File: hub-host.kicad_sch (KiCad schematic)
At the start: 30 parts, among them J1 USB-C USB2.0, Q2 2N7002, U2 USBLC6-2SC6, U22 TLV75533PDBVR, U24 SN74LVC1G04DBVR, U26 TPS2553DBVR, U3 TUSB320LAIRWBR, U45 TLV62568DBVR

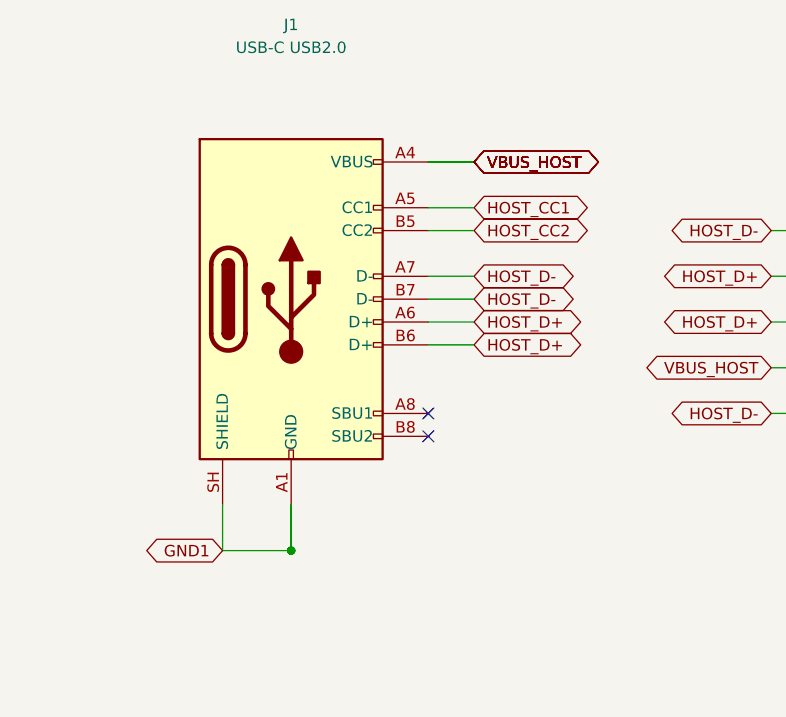
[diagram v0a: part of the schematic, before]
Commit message: feat(revc): assign exact BOM and verified local land patterns
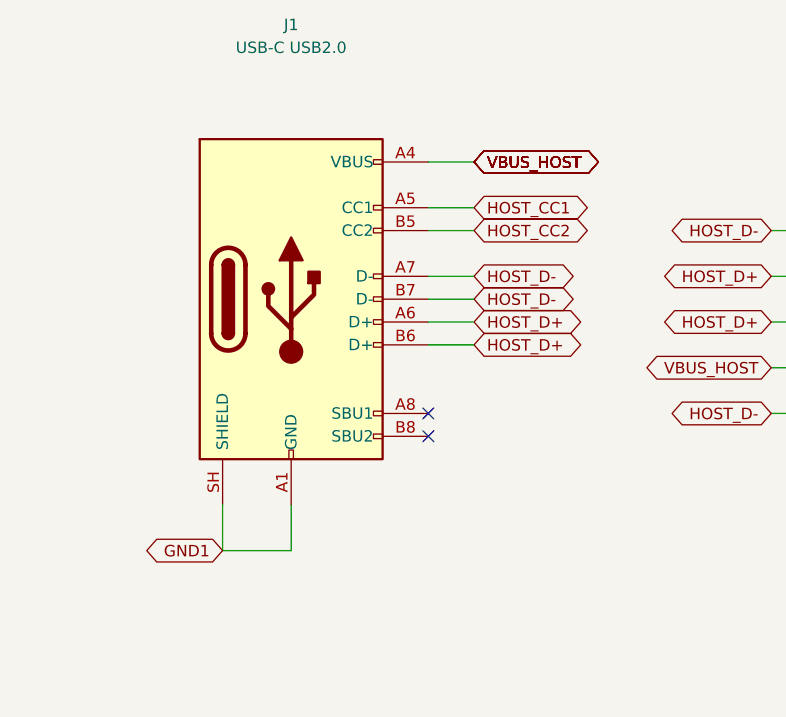
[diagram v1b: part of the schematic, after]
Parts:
- C1, C62, C7, C8: footprint (none) -> hub-lib:C_0402_1005Metric; LCSC (none) -> C77020; MPN (none) -> GRM155R71H104KE14D; Manufacturer (none) -> Murata Manufacturing; Ratings (none) -> 50V X7R 10%
- C113: footprint (none) -> hub-lib:C_0805_2012Metric; LCSC (none) -> C77077; MPN (none) -> GRM21BR61E475KA12L; Manufacturer (none) -> Murata Manufacturing; Ratings (none) -> 25V X5R 10%
- C114: footprint (none) -> hub-lib:C_1210_3225Metric; LCSC (none) -> C21397; MPN (none) -> GRM32ER71E226KE15L; Manufacturer (none) -> Murata Manufacturing; Ratings (none) -> 25V X7R 10%
- C2, C61: footprint (none) -> hub-lib:C_0603_1608Metric; LCSC (none) -> C77046; MPN (none) -> GRM188R61E105KA12D; Manufacturer (none) -> Murata Manufacturing; Ratings (none) -> 25V X5R 10%
- D1: footprint Diode_SMD:D_SOD-523 -> hub-lib:D_SOD-523; LCSC (none) -> C19950551; Ratings (none) -> See exact manufacturer datasheet
- D2: footprint LED_SMD:LED_0603_1608Metric -> hub-lib:LED_0603_1608Metric; LCSC (none) -> C125094; Ratings (none) -> See exact manufacturer datasheet
- J1: footprint Connector_USB:USB_C_Receptacle_HRO_TYPE-C-31-M-12 -> hub-lib:USB_C_Receptacle_HRO_TYPE-C-31-M-12; LCSC (none) -> C165948; Ratings (none) -> See exact manufacturer datasheet
- L4: footprint (none) -> hub-lib:Coilcraft_XFL4020_4x4mm; LCSC (none) -> C122469; Ratings (none) -> See exact manufacturer datasheet
- Q2: footprint Package_TO_SOT_SMD:SOT-23 -> hub-lib:SOT-23; LCSC (none) -> C65189; Ratings (none) -> See exact manufacturer datasheet
- R1: footprint (none) -> hub-lib:R_0402_1005Metric; LCSC (none) -> C2085054; MPN (none) -> ERJ2RKF9093X; Manufacturer (none) -> Panasonic Industry; Ratings (none) -> 1%, 0.1W, 50V
- R114: footprint (none) -> hub-lib:R_0402_1005Metric; LCSC (none) -> C413111; MPN (none) -> ERJ2RKF2003X; Manufacturer (none) -> Panasonic Industry; Ratings (none) -> 1%, 0.1W, 50V
- R115, R4: footprint (none) -> hub-lib:R_0402_1005Metric; LCSC (none) -> C192169; MPN (none) -> ERJ2RKF1003X; Manufacturer (none) -> Panasonic Industry; Ratings (none) -> 1%, 0.1W, 50V
- R2, R3, R6: footprint (none) -> hub-lib:R_0402_1005Metric; LCSC (none) -> C191123; MPN (none) -> ERJ2RKF1002X; Manufacturer (none) -> Panasonic Industry; Ratings (none) -> 1%, 0.1W, 50V
- R5: footprint (none) -> hub-lib:R_0402_1005Metric; MPN (none) -> ERJ2RKF2872X; Manufacturer (none) -> Panasonic Industry; Ratings (none) -> 1%, 0.1W, 50V
- R9: footprint (none) -> hub-lib:R_0402_1005Metric; LCSC (none) -> C409909; MPN (none) -> ERJ2RKF3301X; Manufacturer (none) -> Panasonic Industry; Ratings (none) -> 1%, 0.1W, 50V
- TP1, TP2: footprint TestPoint:TestPoint_Pad_D1.0mm -> hub-lib:TestPoint_Pad_D1.0mm; Manufacturer (none) -> PCB feature; Ratings (none) -> Exposed test pad; no purchased part; now left out of the parts list
- U2: footprint Package_TO_SOT_SMD:SOT-23-6 -> hub-lib:SOT-23-6; LCSC (none) -> C7519; Ratings (none) -> See exact manufacturer datasheet
- U22: footprint (none) -> hub-lib:SOT-23-5; LCSC (none) -> C404027; Ratings (none) -> See exact manufacturer datasheet
- U24: footprint (none) -> hub-lib:SOT-23-5; LCSC (none) -> C7827; Ratings (none) -> See exact manufacturer datasheet
- U26: footprint (none) -> hub-lib:SOT-23-6; LCSC (none) -> C55266; Ratings (none) -> See exact manufacturer datasheet
- U3: footprint (none) -> hub-lib:Texas_X2QFN-12_1.6x1.6mm_P0.4mm; LCSC (none) -> C132554; Ratings (none) -> See exact manufacturer datasheet
- U45: footprint (none) -> hub-lib:SOT-23-5; LCSC (none) -> C163219; Ratings (none) -> See exact manufacturer datasheet

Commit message: feat(revc): place synchronized unrouted board and correct bus startup
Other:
- note added: "CC current qualification: 1.5 A or 3 A required"
- note added: "Declared power origins"
- note added: "Efficient host-core supply: 1.8 V"
- note added: "Host connector and ESD"
- note added: "Isolated-converter input protection"
- note added: "Qualified-host indicator"
- note added: "USB 2.0 / 480 Mbps | Rev C electrical design | Placement and routing review pending"
- note removed: "Rev C | all routing reserved for Alex | electrical draft under review"
- moved on the sheet: C1, C113, C114, C2, C61, C62, C7, C8, D1, D2, J1, L4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

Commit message: feat(revc): finish verified TI hub routing handoff
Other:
- note added: "USB 2.0 / 480 Mbps | Rev C electrical design | Placed PCB; all routing by Alex; hardware tests pending"
- note removed: "USB 2.0 / 480 Mbps | Rev C electrical design | Placement and routing review pending"
- moved on the sheet: D1, D2, Q2
